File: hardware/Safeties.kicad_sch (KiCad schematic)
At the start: 8 parts, among them K4 FINDER-30.22, U14 74AUP1G32

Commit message: Schematic readability update
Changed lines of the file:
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@@
     (effects (font (size 1.27 1.27)) (justify left bottom))
-  )
-  (global_label "SAFETY_AIR" (shape input) (at 63.5 46.355 0) (fields_autoplaced)
-    (effects (font (size 1.27 1.27)) (justify left))
-    (property "Intersheet References" "${INTERSHEET_REFS}" (id 0) (at 76.3471 46.2756 0)
-      (effects (font (size 1.27 1.27)) (justify left) hide)
-    )
-  )
-  (global_label "AMS_SAFETY_1" (shape input) (at 208.915 50.8 180) (fields_autoplaced)
-    (effects (font (size 1.27 1.27)) (justify right))
-    (property "Intersheet References" "${INTERSHEET_REFS}" (id 0) (at 193.1046 50.7206 0)
-      (effects (font (size 1.27 1.27)) (justify right) hide)
-    )
   )
   (global_label "AIR_M" (shape input) (at 63.5 63.5 0) (fields_autoplaced)
     (effects (font (size 1.27 1.27)) (justify left))
     (property "Intersheet References" "${INTERSHEET_REFS}" (id 0) (at 71.2066 63.4206 0)
-      (effects (font (size 1.27 1.27)) (justify left) hide)
-    )
-  )
-  (global_label "SAFETY_DETECTION" (shape input) (at 59.055 161.925 0) (fields_autoplaced)
-    (effects (font (size 1.27 1.27)) (justify left))
-    (property "Intersheet References" "${INTERSHEET_REFS}" (id 0) (at 78.9778 161.8456 0)
-      (effects (font (size 1.27 1.27)) (justify left) hide)
-    )
-  )
-  (global_label "AMS_FAULT_COCKPIT" (shape input) (at 208.915 60.96 180) (fields_autoplaced)
-    (effects (font (size 1.27 1.27)) (justify right))
-    (property "Intersheet References" "${INTERSHEET_REFS}" (id 0) (at 187.4198 61.0394 0)
-      (effects (font (size 1.27 1.27)) (justify right) hide)
-    )
-  )
-  (global_label "AIR_P" (shape input) (at 63.5 78.74 0) (fields_autoplaced)
-    (effects (font (size 1.27 1.27)) (justify left))
-    (property "Intersheet References" "${INTERSHEET_REFS}" (id 0) (at 71.0252 78.6606 0)
-      (effects (font (size 1.27 1.27)) (justify left) hide)
-    )
-  )
-  (global_label "SAFETY_AIR" (shape input) (at 30.48 161.925 180) (fields_autoplaced)
-    (effects (font (size 1.27 1.27)) (justify right))
-    (property "Intersheet References" "${INTERSHEET_REFS}" (id 0) (at 17.6329 162.0044 0)
-      (effects (font (size 1.27 1.27)) (justify right) hide)
-    )
-  )
-  (global_label "AIR_PRE" (shape input) (at 63.5 48.895 0) (fields_autoplaced)
-    (effects (font (size 1.27 1.27)) (justify left))
-    (property "Intersheet References" "${INTERSHEET_REFS}" (id 0) (at 73.4442 48.8156 0)
       (effects (font (size 1.27 1.27)) (justify left) hide)
     )
@@
     )
   )
-  (global_label "SIGNAL_AIR_PRE" (shape input) (at 37.465 48.895 180) (fields_autoplaced)
+  (global_label "AIR_PRE" (shape input) (at 63.5 48.895 0) (fields_autoplaced)
+    (effects (font (size 1.27 1.27)) (justify left))
+    (property "Intersheet References" "${INTERSHEET_REFS}" (id 0) (at 73.4442 48.8156 0)
+      (effects (font (size 1.27 1.27)) (justify left) hide)
+    )
+  )
+  (global_label "AMS_FAULT_COCKPIT" (shape input) (at 208.915 60.96 180) (fields_autoplaced)
     (effects (font (size 1.27 1.27)) (justify right))
-    (property "Intersheet References" "${INTERSHEET_REFS}" (id 0) (at 20.0218 48.8156 0)
+    (property "Intersheet References" "${INTERSHEET_REFS}" (id 0) (at 187.4198 60.8806 0)
       (effects (font (size 1.27 1.27)) (justify right) hide)
     )
   )
-  (global_label "SIGNAL_AIR_M" (shape input) (at 37.465 63.5 180) (fields_autoplaced)
+  (global_label "AMS_SAFETY_1" (shape input) (at 208.915 50.8 180) (fields_autoplaced)
     (effects (font (size 1.27 1.27)) (justify right))
-    (property "Intersheet References" "${INTERSHEET_REFS}" (id 0) (at 22.2594 63.4206 0)
+    (property "Intersheet References" "${INTERSHEET_REFS}" (id 0) (at 193.1046 50.7206 0)
       (effects (font (size 1.27 1.27)) (justify right) hide)
     )
   )
-  (global_label "SIGNAL_AIR_P" (shape input) (at 37.465 78.74 180) (fields_autoplaced)
+  (global_label "SAFETY_AIR" (shape input) (at 63.5 46.355 0) (fields_autoplaced)
+    (effects (font (size 1.27 1.27)) (justify left))
+    (property "Intersheet References" "${INTERSHEET_REFS}" (id 0) (at 76.3471 46.2756 0)
+      (effects (font (size 1.27 1.27)) (justify left) hide)
+    )
+  )
+  (global_label "SAFETY_AIR" (shape input) (at 30.48 161.925 180) (fields_autoplaced)
     (effects (font (size 1.27 1.27)) (justify right))
-    (property "Intersheet References" "${INTERSHEET_REFS}" (id 0) (at 22.4408 78.6606 0)
+    (property "Intersheet References" "${INTERSHEET_REFS}" (id 0) (at 17.6329 161.8456 0)
       (effects (font (size 1.27 1.27)) (justify right) hide)
     )
@@
     )
   )
-  (global_label "AMS_FAULT_MCU" (shape input) (at 127 109.22 180) (fields_autoplaced)
-    (effects (font (size 1.27 1.27)) (justify right))
-    (property "Intersheet References" "${INTERSHEET_REFS}" (id 0) (at 109.4358 109.1406 0)
-      (effects (font (size 1.27 1.27)) (justify right) hide)
+  (global_label "AIR_P" (shape input) (at 63.5 78.74 0) (fields_autoplaced)
+    (effects (font (size 1.27 1.27)) (justify left))
+    (property "Intersheet References" "${INTERSHEET_REFS}" (id 0) (at 71.0252 78.6606 0)
+      (effects (font (size 1.27 1.27)) (justify left) hide)
     )
   )
+  (hierarchical_label "SIGNAL_AIR_M" (shape input) (at 37.465 63.5 180)
+    (effects (font (size 1.27 1.27)) (justify right))
+  )
+  (hierarchical_label "SIGNAL_AIR_P" (shape input) (at 37.465 78.74 180)
+    (effects (font (size 1.27 1.27)) (justify right))
+  )
+  (hierarchical_label "AMS_FAULT_MCU" (shape input) (at 127 109.22 180)
+    (effects (font (size 1.27 1.27)) (justify right))
+  )
+  (hierarchical_label "SIGNAL_AIR_PRE" (shape input) (at 37.465 48.895 180)
+    (effects (font (size 1.27 1.27)) (justify right))
+  )
+  (hierarchical_label "SAFETY_DETECTION" (shape input) (at 59.055 161.925 0)
+    (effects (font (size 1.27 1.27)) (justify left))
+  )
   (symbol (lib_id "power:GND") (at 62.23 92.075 0) (unit 1)

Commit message: finished board design
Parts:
- removed C10: 100uF/35V, Capacitor_SMD:CP_Elec_8x10, symbol Device:CP_Small
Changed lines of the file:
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@@
   (junction (at 163.195 110.49) (diameter 0) (color 0 0 0 0)
   )
-  (junction (at 62.23 60.96) (diameter 0) (color 0 0 0 0)
-  )
-  (junction (at 62.23 76.2) (diameter 0) (color 0 0 0 0)
-  )
   (junction (at 134.62 109.22) (diameter 0) (color 0 0 0 0)
-  )
-  (junction (at 62.23 46.355) (diameter 0) (color 0 0 0 0)
   )
   (junction (at 143.51 116.84) (diameter 0) (color 0 0 0 0)
@@
     (stroke (width 0) (type default) (color 0 0 0 0))
   )
-  (wire (pts (xy 62.23 46.355) (xy 63.5 46.355))
+  (wire (pts (xy 60.96 46.355) (xy 63.5 46.355))
     (stroke (width 0) (type default) (color 0 0 0 0))
   )
@@
     (stroke (width 0) (type default) (color 0 0 0 0))
   )
-  (wire (pts (xy 62.23 76.2) (xy 62.23 85.725))
-    (stroke (width 0) (type default) (color 0 0 0 0))
-  )
   (wire (pts (xy 154.94 99.06) (xy 154.94 107.95))
     (stroke (width 0) (type default) (color 0 0 0 0))
@@
     (stroke (width 0) (type default) (color 0 0 0 0))
   )
-  (wire (pts (xy 62.23 60.96) (xy 63.5 60.96))
+  (wire (pts (xy 60.96 60.96) (xy 63.5 60.96))
     (stroke (width 0) (type default) (color 0 0 0 0))
   )
@@
     (stroke (width 0) (type default) (color 0 0 0 0))
   )
-  (wire (pts (xy 60.96 46.355) (xy 62.23 46.355))
-    (stroke (width 0) (type default) (color 0 0 0 0))
-  )
   (polyline (pts (xy 163.195 119.38) (xy 163.83 119.38))
-    (stroke (width 0) (type default) (color 0 0 0 0))
-  )
-  (wire (pts (xy 62.23 90.805) (xy 62.23 92.075))
     (stroke (width 0) (type default) (color 0 0 0 0))
   )
@@
     (stroke (width 0) (type default) (color 0 0 0 0))
   )
-  (wire (pts (xy 62.23 60.96) (xy 62.23 76.2))
-    (stroke (width 0) (type default) (color 0 0 0 0))
-  )
   (wire (pts (xy 227.965 38.735) (xy 227.965 58.42))
     (stroke (width 0) (type default) (color 0 0 0 0))
@@
     (stroke (width 0) (type default) (color 0 0 0 0))
   )
-  (wire (pts (xy 60.96 60.96) (xy 62.23 60.96))
-    (stroke (width 0) (type default) (color 0 0 0 0))
-  )
   (wire (pts (xy 133.35 109.22) (xy 134.62 109.22))
     (stroke (width 0) (type default) (color 0 0 0 0))
@@
   )
   (wire (pts (xy 60.96 63.5) (xy 63.5 63.5))
-    (stroke (width 0) (type default) (color 0 0 0 0))
-  )
-  (wire (pts (xy 62.23 46.355) (xy 62.23 60.96))
     (stroke (width 0) (type default) (color 0 0 0 0))
   )
@@
     (stroke (width 0) (type default) (color 0 0 0 0))
   )
-  (wire (pts (xy 62.23 76.2) (xy 63.5 76.2))
-    (stroke (width 0) (type default) (color 0 0 0 0))
-  )
   (wire (pts (xy 60.96 48.895) (xy 63.5 48.895))
     (stroke (width 0) (type default) (color 0 0 0 0))
@@
     (stroke (width 0) (type default) (color 0 0 0 0))
   )
-  (wire (pts (xy 60.96 76.2) (xy 62.23 76.2))
+  (wire (pts (xy 60.96 76.2) (xy 63.5 76.2))
     (stroke (width 0) (type default) (color 0 0 0 0))
   )
@@
   (hierarchical_label "SAFETY_DETECTION" (shape input) (at 59.055 161.925 0)
     (effects (font (size 1.27 1.27)) (justify left))
-  )
-  (symbol (lib_id "power:GND") (at 62.23 92.075 0) (unit 1)
-    (in_bom yes) (on_board yes)
-    (property "Reference" "#PWR024" (id 0) (at 62.23 98.425 0)
-      (effects (font (size 1.27 1.27)) hide)
-    )
-    (property "Value" "GND" (id 1) (at 62.357 96.4692 0))
-    (property "Footprint" "" (id 2) (at 62.23 92.075 0)
-      (effects (font (size 1.27 1.27)) hide)
-    )
-    (property "Datasheet" "" (id 3) (at 62.23 92.075 0)
-      (effects (font (size 1.27 1.27)) hide)
-    )
-    (pin "1")
   )
   (symbol (lib_id "power:+5V") (at 210.185 38.1 0) (unit 1)
@@
     (pin "1")
   )
-  (symbol (lib_id "Device:CP_Small") (at 62.23 88.265 0) (unit 1)
-    (in_bom yes) (on_board yes)
-    (property "Reference" "C10" (id 0) (at 64.4652 87.0966 0)
-      (effects (font (size 1.27 1.27)) (justify left))
-    )
-    (property "Value" "100uF/35V" (id 1) (at 64.4652 89.408 0)
-      (effects (font (size 1.27 1.27)) (justify left))
-    )
-    (property "Footprint" "Capacitor_SMD:CP_Elec_8x10" (id 2) (at 62.23 88.265 0)
-      (effects (font (size 1.27 1.27)) hide)
-    )
-    (property "Datasheet" "~" (id 3) (at 62.23 88.265 0)
-      (effects (font (size 1.27 1.27)) hide)
-    )
-    (pin "1")
-    (pin "2")
-  )
   (symbol (lib_id "Device:R_Small") (at 134.62 113.03 180) (unit 1)

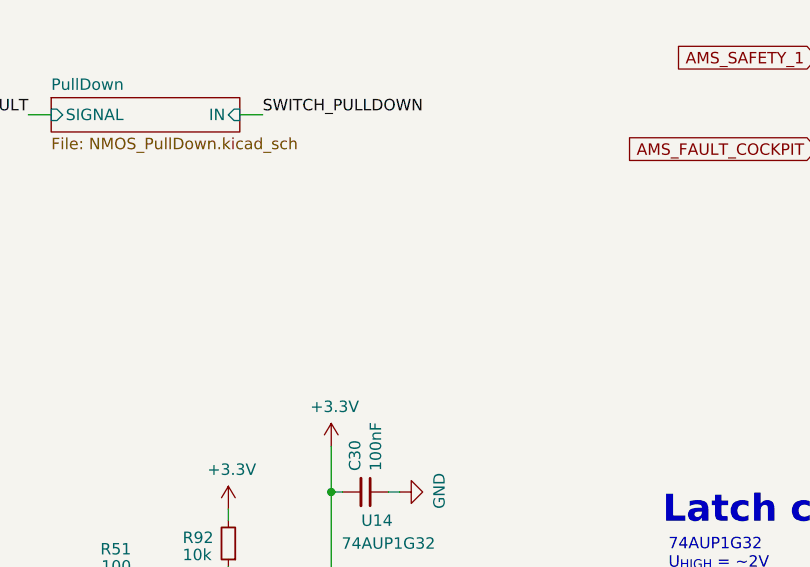
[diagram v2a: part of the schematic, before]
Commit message: added missing led for safety indication
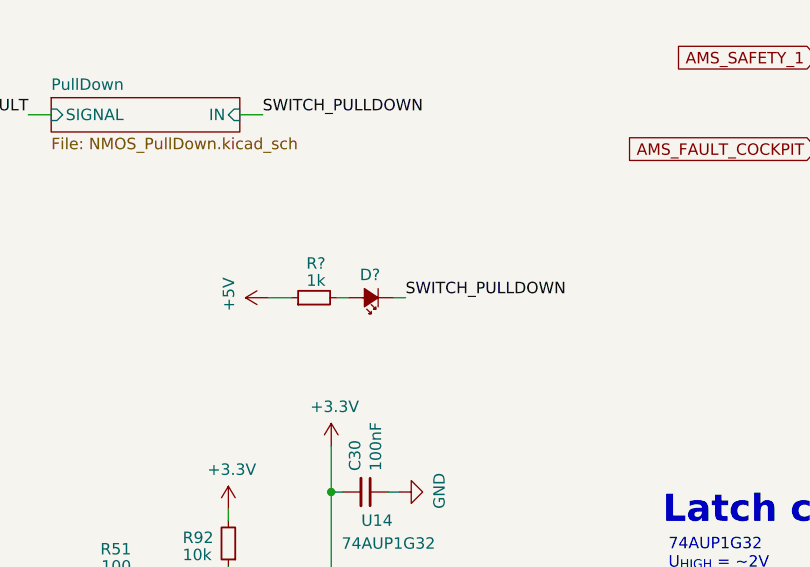
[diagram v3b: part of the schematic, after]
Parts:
- added D?: LED_Small_ALT, LED_SMD:LED_0603_1608Metric, symbol Device:LED_Small_ALT
- added R?: 1k, Resistor_SMD:R_0603_1608Metric, symbol Device:R_Small
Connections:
- net +5V: now also R?.1
- net SWITCH_PULLDOWN: now also D?.1 (K)
- new net: D?.2 (A), R?.2
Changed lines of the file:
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@@
     (stroke (width 1) (type default) (color 132 0 0 1))
   )
+  (wire (pts (xy 150.495 77.47) (xy 147.955 77.47))
+    (stroke (width 0) (type default) (color 0 0 0 0))
+  )
   (wire (pts (xy 208.915 50.8) (xy 211.455 50.8))
     (stroke (width 0) (type default) (color 0 0 0 0))
   )
+  (wire (pts (xy 156.845 77.47) (xy 155.575 77.47))
+    (stroke (width 0) (type default) (color 0 0 0 0))
+  )
   (polyline (pts (xy 163.195 114.3) (xy 163.195 115.57))
     (stroke (width 0) (type default) (color 0 0 0 0))
@@
   )
   (wire (pts (xy 37.465 63.5) (xy 40.005 63.5))
+    (stroke (width 0) (type default) (color 0 0 0 0))
+  )
+  (wire (pts (xy 163.195 77.47) (xy 161.925 77.47))
     (stroke (width 0) (type default) (color 0 0 0 0))
   )
@@
     (effects (font (size 1.27 1.27)) (justify left bottom))
   )
+  (label "SWITCH_PULLDOWN" (at 163.195 77.47 0)
+    (effects (font (size 1.27 1.27)) (justify left bottom))
+  )
   (label "AMS_FAULT" (at 165.1 110.49 0)
     (effects (font (size 1.27 1.27)) (justify left bottom))
@@
     (pin "1")
   )
+  (symbol (lib_id "Device:LED_Small_ALT") (at 159.385 77.47 180) (unit 1)
+    (in_bom yes) (on_board yes)
+    (property "Reference" "D?" (id 0) (at 158.115 74.93 0)
+      (effects (font (size 1.27 1.27)) (justify right))
+    )
+    (property "Value" "LED_Small_ALT" (id 1) (at 159.385 81.1276 0)
+      (effects (font (size 1.27 1.27)) hide)
+    )
+    (property "Footprint" "LED_SMD:LED_0603_1608Metric" (id 2) (at 159.385 77.47 90)
+      (effects (font (size 1.27 1.27)) hide)
+    )
+    (property "Datasheet" "~" (id 3) (at 159.385 77.47 90)
+      (effects (font (size 1.27 1.27)) hide)
+    )
+    (pin "1")
+    (pin "2")
+  )
+  (symbol (lib_id "Device:R_Small") (at 153.035 77.47 90) (unit 1)
+    (in_bom yes) (on_board yes)
+    (property "Reference" "R?" (id 0) (at 154.305 73.66 90)
+      (effects (font (size 1.27 1.27)) (justify left))
+    )
+    (property "Value" "1k" (id 1) (at 154.305 75.565 90)
+      (effects (font (size 1.27 1.27)) (justify left))
+    )
+    (property "Footprint" "Resistor_SMD:R_0603_1608Metric" (id 2) (at 153.035 77.47 0)
+      (effects (font (size 1.27 1.27)) hide)
+    )
+    (property "Datasheet" "~" (id 3) (at 153.035 77.47 0)
+      (effects (font (size 1.27 1.27)) hide)
+    )
+    (pin "1")
+    (pin "2")
+  )
   (symbol (lib_id "Device:R_Small") (at 143.51 104.775 180) (unit 1)
     (in_bom yes) (on_board yes)
@@
     (pin "2")
   )
+  (symbol (lib_id "power:+5V") (at 147.955 77.47 90) (unit 1)
+    (in_bom yes) (on_board yes)
+    (property "Reference" "#PWR?" (id 0) (at 151.765 77.47 0)
+      (effects (font (size 1.27 1.27)) hide)
+    )
+    (property "Value" "+5V" (id 1) (at 143.5608 77.089 0))
+    (property "Footprint" "" (id 2) (at 147.955 77.47 0)
+      (effects (font (size 1.27 1.27)) hide)
+    )
+    (property "Datasheet" "" (id 3) (at 147.955 77.47 0)
+      (effects (font (size 1.27 1.27)) hide)
+    )
+    (pin "1")
+  )
   (symbol (lib_id "power:+3.3V") (at 143.51 100.965 0) (unit 1)

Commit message: sync
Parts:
- gave numbers to parts that had none: 2
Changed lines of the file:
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@@
   (symbol (lib_id "Device:LED_Small_ALT") (at 159.385 77.47 180) (unit 1)
     (in_bom yes) (on_board yes)
-    (property "Reference" "D?" (id 0) (at 158.115 74.93 0)
+    (property "Reference" "D9" (id 0) (at 158.115 74.93 0)
       (effects (font (size 1.27 1.27)) (justify right))
     )
@@
   (symbol (lib_id "Device:R_Small") (at 153.035 77.47 90) (unit 1)
     (in_bom yes) (on_board yes)
-    (property "Reference" "R?" (id 0) (at 154.305 73.66 90)
+    (property "Reference" "R77" (id 0) (at 154.305 73.66 90)
       (effects (font (size 1.27 1.27)) (justify left))
     )
@@
   (symbol (lib_id "power:+5V") (at 147.955 77.47 90) (unit 1)
     (in_bom yes) (on_board yes)
-    (property "Reference" "#PWR?" (id 0) (at 151.765 77.47 0)
+    (property "Reference" "#PWR0192" (id 0) (at 151.765 77.47 0)
       (effects (font (size 1.27 1.27)) hide)
     )

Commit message: schematic override, just cuz
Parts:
- removed K4: FINDER-30.22, Relay_THT:Relay_DPDT_Finder_30.22, symbol Relay:FINDER-30.22
- added Q1, Q2: 2N7002, Package_TO_SOT_SMD:SOT-23, symbol Transistor_FET:2N7002
- added R17: 10k, Resistor_SMD:R_0603_1608Metric, symbol Device:R_Small
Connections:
- net +5V: now also Q2.3 (D), R17.1
- net AMS_FAULT_COCKPIT: now also Q2.2 (S)
- net AMS_SAFETY_1: now also Q1.3 (D)
- net AMS_SAFETY_2: now also Q1.2 (S)
- net SWITCH_PULLDOWN: now also Q1.1 (G), Q2.1 (G), R17.2
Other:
- removed sheet Air M
- removed sheet Air P
- removed sheet Air pre
- added sheet HP_PullDown (HP_NMOS_PullDown.kicad_sch)
- added sheet HP_PullDown1 (HP_NMOS_PullDown.kicad_sch)
- added sheet HP_PullDown2 (HP_NMOS_PullDown.kicad_sch)
- moved on the sheet: C25, C30, D9, R51, R52, R77, R92, U14
